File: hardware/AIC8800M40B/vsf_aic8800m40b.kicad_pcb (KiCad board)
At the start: 4 copper layers, 36.8 x 57.2 mm, 87 parts, among them J1 USB_A, J2 USB_C_Receptacle_USB2.0, J3 USB_C_Receptacle_USB2.0, J4 Micro_SD_Card_Det1, J6 Conn_Coaxial, J7 Conn_Coaxial, J8 Conn_02x15_Odd_Even, Q1 S9013, SW1 SW_Push, SW2 SW_Push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

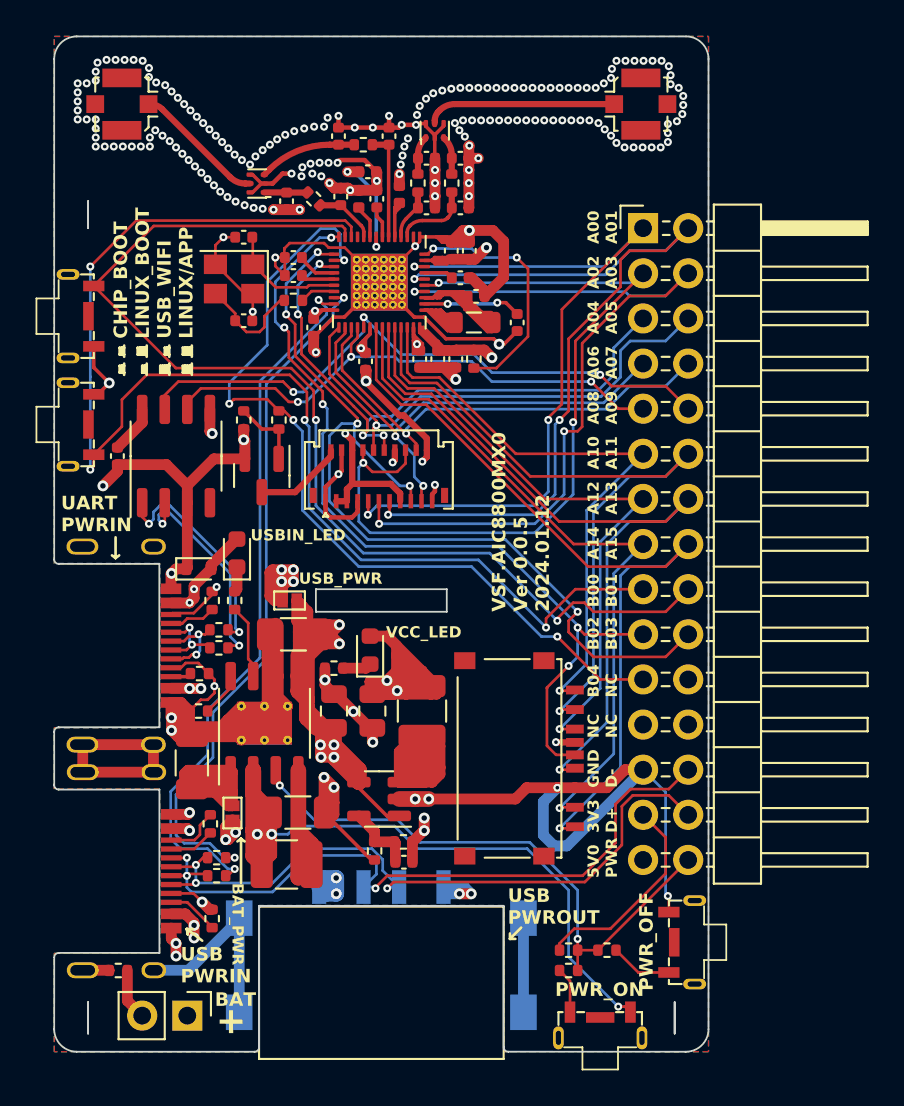
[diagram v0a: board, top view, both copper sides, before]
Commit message: [hardware/aic8800m40b] add level converter for debug uart
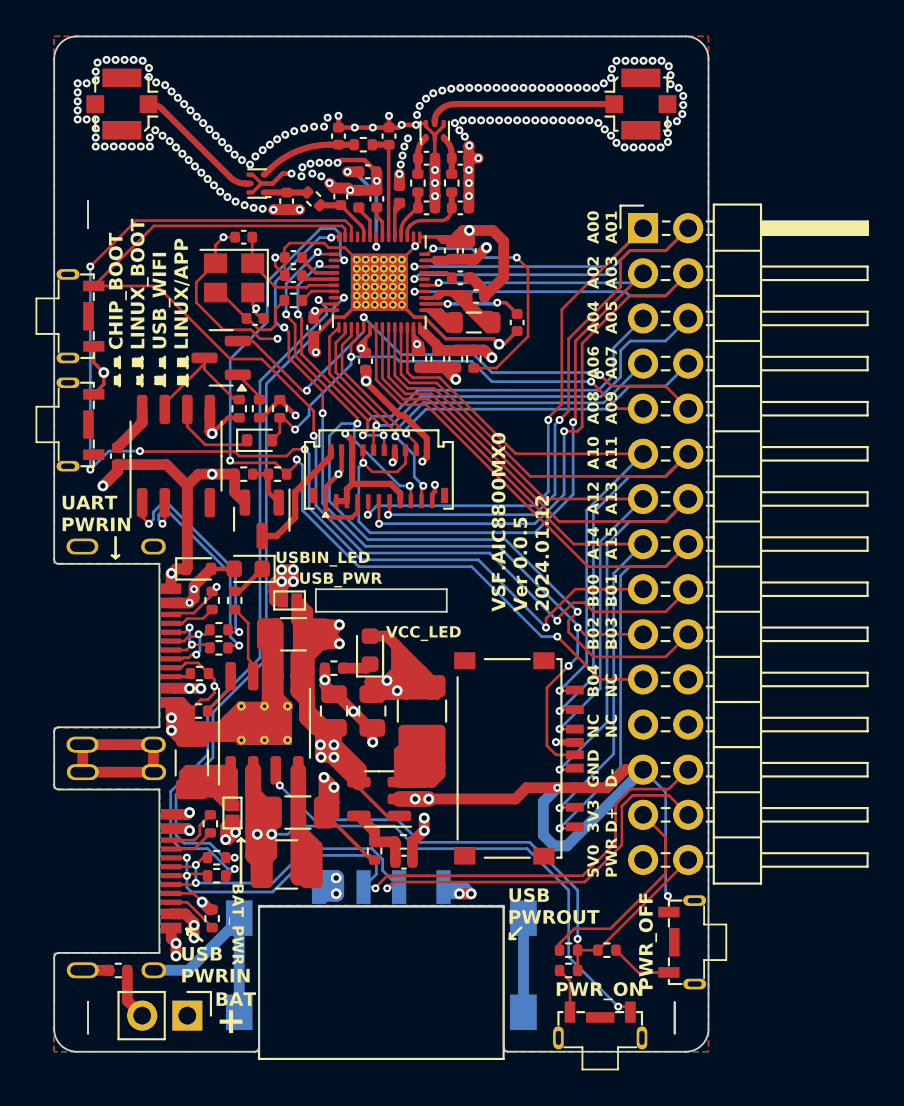
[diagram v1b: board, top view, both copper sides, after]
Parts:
- added D4: 1N4148, Diode_SMD:D_SOD-523, F.Cu at (214.8, 118.0)
- added Q2: PMBT3904, Package_TO_SOT_SMD:SOT-23, F.Cu at (212.6, 113.3)
- added R26: 4.7K, Resistor_SMD:R_0402_1005Metric, F.Cu at (215.9, 116.2)
- added R27: 4.7K, Resistor_SMD:R_0402_1005Metric, F.Cu at (213.6, 116.2)
- added R28: 4.7K, Resistor_SMD:R_0402_1005Metric, F.Cu at (214.8, 116.2)
- moved R17 3.05 mm to (215.8, 119.9), turned to 180 degrees
- moved R16 3.05 mm to (213.9, 119.9), turned to 180 degrees
- moved Q1 2.46 mm to (214.9, 122.4)
- moved D2 1.09 mm to (214.1, 125.2), turned to 180 degrees
- moved C30 0.65 mm to (214.5, 111.1)
- moved Y1 0.06 mm to (213.3, 108.8)
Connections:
- U2 pad 6: /GPIOA8 -> Net-(D4-K)
- U2 pad 7: /GPIOA9 -> Net-(Q2-C)
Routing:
- net GND: track 342.0 -> 349.7 mm, vias 207 -> 208
- net Net-(Q2-C): track 0.00 -> 7.14 mm
- net /PWR_3V3: track 150.5 -> 156.6 mm, vias 9 -> 10
- net /GPIOB0: track 73.5 -> 67.8 mm, vias 4 -> 5
- net Net-(D4-K): track 0.00 -> 4.86 mm
- net /GPIOA9: track 35.7 -> 31.5 mm
- net /GPIOA8: track 30.8 -> 27.4 mm
- net Net-(Q2-B): track 0.00 -> 1.90 mm
- net Net-(J5-LEDK): track 5.08 -> 6.93 mm
- net Net-(Q1-B): track 4.09 -> 2.75 mm
- net /GPIOB4: track 48.0 -> 49.2 mm
- net /GPIOB1: track 62.3 -> 61.6 mm
- net Net-(D2-K): track 1.42 -> 2.07 mm

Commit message: [hardware/aic8800m40b] update pcb version and date
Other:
- board text added: "VSF.AIC8800MX0 Ver 0.0.6 2024.11.28"
- board text removed: "VSF.AIC8800MX0 Ver 0.0.5 2024.01.12"
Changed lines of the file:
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@@
 		(tags "LED")
 		(property "Reference" "D2"
-			(at 0 -1.43 360)
+			(at 0 -1.43 0)
 			(layer "F.SilkS")
 			(hide yes)
@@
 		)
 		(property "Value" "LED, RED"
-			(at 0 1.43 360)
+			(at 0 1.43 0)
 			(layer "F.Fab")
 			(effects
@@
 		)
 		(property "Footprint" "LED_SMD:LED_0603_1608Metric"
-			(at 0 0 360)
+			(at 0 0 0)
 			(layer "F.Fab")
 			(hide yes)
@@
 		)
 		(property "Datasheet" ""
-			(at 0 0 360)
+			(at 0 0 0)
 			(layer "F.Fab")
 			(hide yes)
@@
 		)
 		(property "Description" ""
-			(at 0 0 360)
+			(at 0 0 0)
 			(layer "F.Fab")
 			(hide yes)
@@
 		)
 		(fp_text user "${REFERENCE}"
-			(at 0 0 360)
+			(at 0 0 0)
 			(layer "F.Fab")
 			(effects
@@
 		(tags "resistor")
 		(property "Reference" "R17"
-			(at 0 -1.1684 360)
+			(at 0 -1.1684 0)
 			(layer "F.SilkS")
 			(hide yes)
@@
 		)
 		(property "Value" "1k"
-			(at 0 1.17 360)
+			(at 0 1.17 0)
 			(layer "F.Fab")
 			(effects
@@
 		)
 		(property "Footprint" "Resistor_SMD:R_0402_1005Metric"
-			(at 0 0 360)
+			(at 0 0 0)
 			(layer "F.Fab")
 			(hide yes)
@@
 		)
 		(property "Datasheet" ""
-			(at 0 0 360)
+			(at 0 0 0)
 			(layer "F.Fab")
 			(hide yes)
@@
 		)
 		(property "Description" ""
-			(at 0 0 360)
+			(at 0 0 0)
 			(layer "F.Fab")
 			(hide yes)
@@
 		)
 		(fp_text user "${REFERENCE}"
-			(at 0 0 360)
+			(at 0 0 0)
 			(layer "F.Fab")
 			(effects
@@
 		(tags "SOT TO_SOT_SMD")
 		(property "Reference" "Q2"
-			(at 0 -2.4 360)
+			(at 0 -2.4 0)
 			(layer "F.SilkS")
 			(hide yes)
@@
 		)
 		(property "Value" "PMBT3904"
-			(at 0 2.4 360)
+			(at 0 2.4 0)
 			(layer "F.Fab")
 			(effects
@@
 		)
 		(fp_text user "${REFERENCE}"
-			(at 0 0 360)
+			(at 0 0 0)
 			(layer "F.Fab")
 			(effects
@@
 		(tags "resistor")
 		(property "Reference" "R16"
-			(at -2.032 0 360)
+			(at -2.032 0 0)
 			(layer "F.SilkS")
 			(hide yes)
@@
 		)
 		(property "Value" "3.3k"
-			(at 0 1.17 360)
+			(at 0 1.17 0)
 			(layer "F.Fab")
 			(effects
@@
 		)
 		(property "Footprint" "Resistor_SMD:R_0402_1005Metric"
-			(at 0 0 360)
+			(at 0 0 0)
 			(layer "F.Fab")
 			(hide yes)
@@
 		)
 		(property "Datasheet" ""
-			(at 0 0 360)
+			(at 0 0 0)
 			(layer "F.Fab")
 			(hide yes)
@@
 		)
 		(property "Description" ""
-			(at 0 0 360)
+			(at 0 0 0)
 			(layer "F.Fab")
 			(hide yes)
@@
 		)
 		(fp_text user "${REFERENCE}"
-			(at 0 0 360)
+			(at 0 0 0)
 			(layer "F.Fab")
 			(effects
@@
 		(tags "resistor")
 		(property "Reference" "R26"
-			(at 1.397 -0.381 360)
+			(at 1.397 -0.381 0)
 			(layer "F.SilkS")
 			(hide yes)
@@
 		)
 	)
-	(gr_text "VSF.AIC8800MX0\nVer 0.0.5\n2024.01.12"
+	(gr_text "VSF.AIC8800MX0\nVer 0.0.6\n2024.11.28"
 		(at 231.14 127.635 90)
 		(layer "F.SilkS")

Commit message: [hardware/aic8800m40b] update
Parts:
- C30: value 0Ohm -> NC
- D4: value 1N4148 -> PMEG1030EJ; footprint Diode_SMD:D_SOD-523 -> Diode_SMD:D_SOD-323
- R23: value NC -> 0Ohm
- moved D4 0.26 mm to (214.8, 118.2)
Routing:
- net /GPIOB4: track 49.2 -> 49.8 mm
